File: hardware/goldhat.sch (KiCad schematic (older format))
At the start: 3 parts

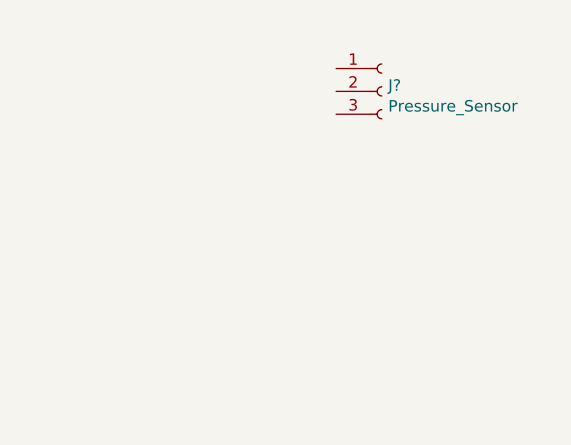
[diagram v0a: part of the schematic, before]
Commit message: added motor connectors
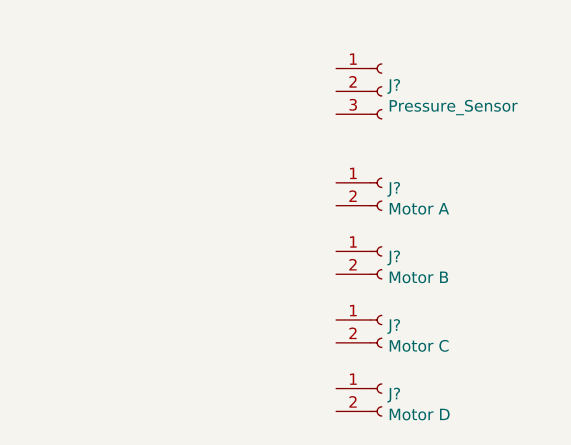
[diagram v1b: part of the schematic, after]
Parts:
- added J?: Motor A, symbol Connector:Conn_01x02_Female
- added J?: Motor B, symbol Connector:Conn_01x02_Female
- added J?: Motor C, symbol Connector:Conn_01x02_Female
- added J?: Motor D, symbol Connector:Conn_01x02_Female
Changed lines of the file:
@@
+	1    0    0    -1
+$EndComp
+$Comp
+L Connector:Conn_01x02_Female J?
+U 1 1 5E94AC7A
+P 9800 5200
+F 0 "J?" H 9828 5176 50  0000 L CNN
+F 1 "Motor A" H 9828 5085 50  0000 L CNN
+F 2 "" H 9800 5200 50  0001 C CNN
+F 3 "~" H 9800 5200 50  0001 C CNN
+	1    9800 5200
+	1    0    0    -1
+$EndComp
+$Comp
+L Connector:Conn_01x02_Female J?
+U 1 1 5E94B72C
+P 9800 5500
+F 0 "J?" H 9828 5476 50  0000 L CNN
+F 1 "Motor B" H 9828 5385 50  0000 L CNN
+F 2 "" H 9800 5500 50  0001 C CNN
+F 3 "~" H 9800 5500 50  0001 C CNN
+	1    9800 5500
+	1    0    0    -1
+$EndComp
+$Comp
+L Connector:Conn_01x02_Female J?
+U 1 1 5E94CD4B
+P 9800 5800
+F 0 "J?" H 9828 5776 50  0000 L CNN
+F 1 "Motor C" H 9828 5685 50  0000 L CNN
+F 2 "" H 9800 5800 50  0001 C CNN
+F 3 "~" H 9800 5800 50  0001 C CNN
+	1    9800 5800
+	1    0    0    -1
+$EndComp
+$Comp
+L Connector:Conn_01x02_Female J?
+U 1 1 5E94CD51
+P 9800 6100
+F 0 "J?" H 9828 6076 50  0000 L CNN
+F 1 "Motor D" H 9828 5985 50  0000 L CNN
+F 2 "" H 9800 6100 50  0001 C CNN
+F 3 "~" H 9800 6100 50  0001 C CNN
+	1    9800 6100
 	1    0    0    -1
 $EndComp

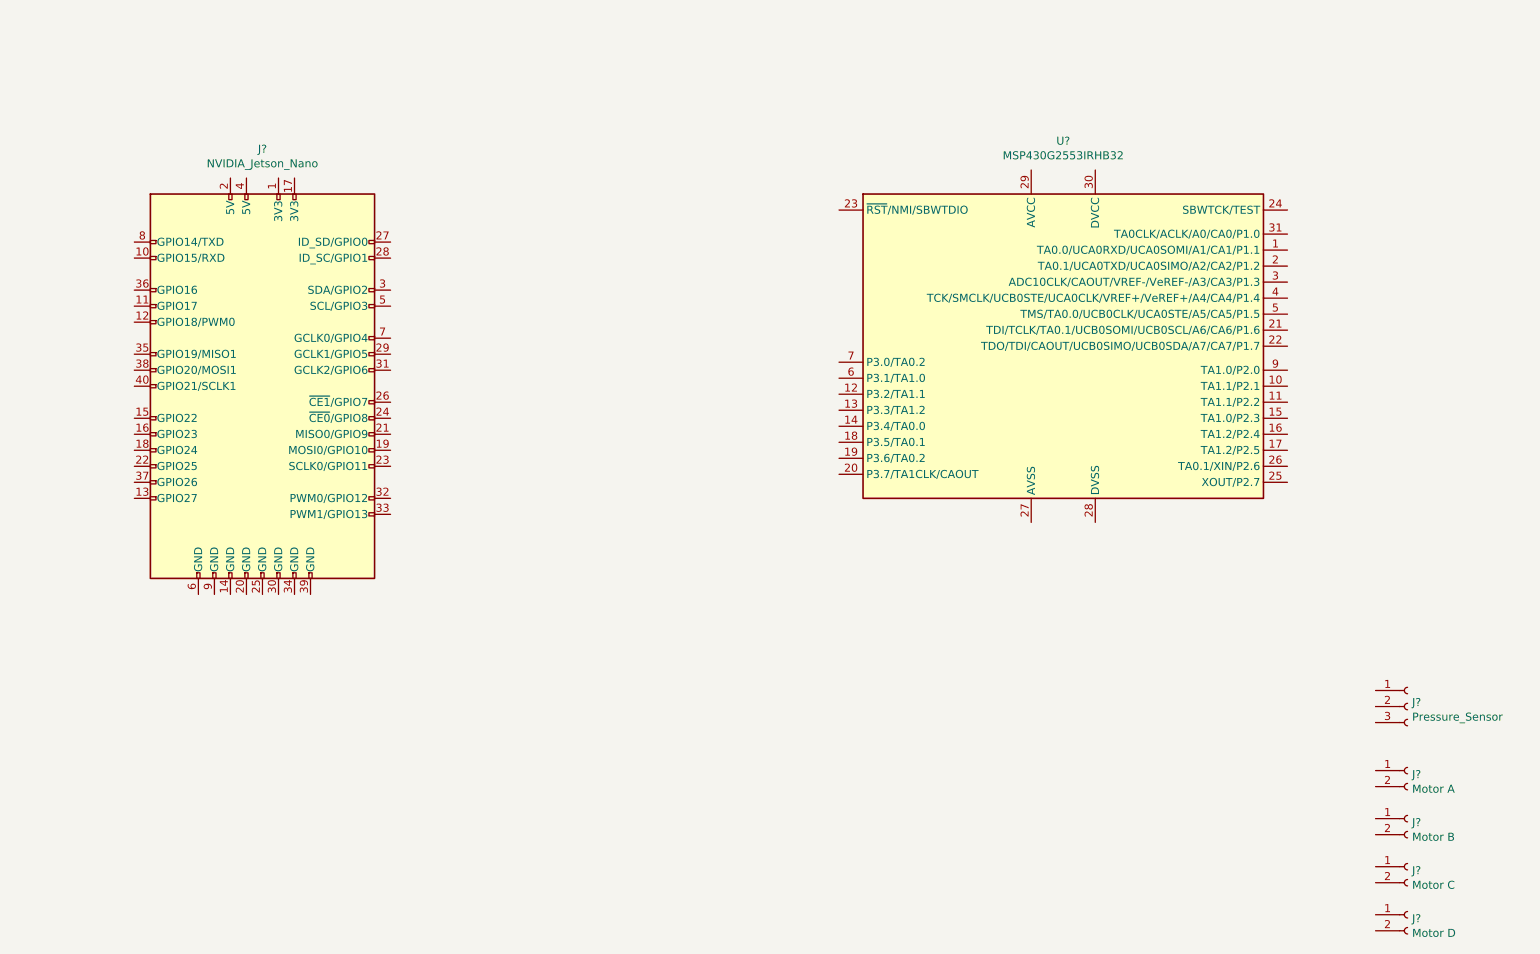
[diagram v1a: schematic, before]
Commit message: added hierarchical sheets because organizing
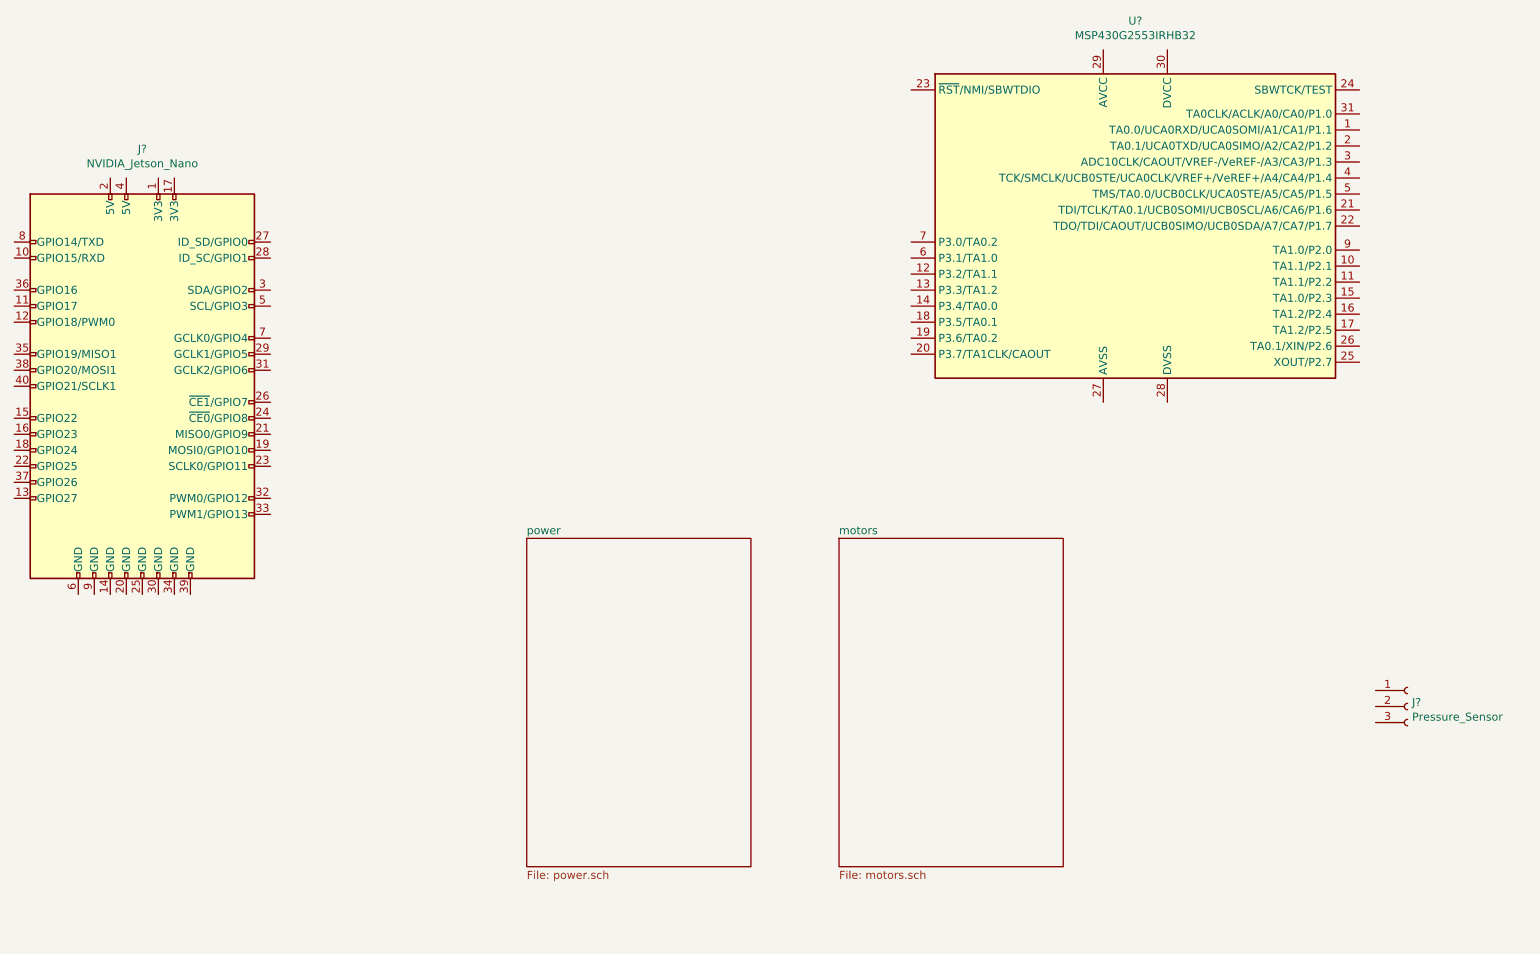
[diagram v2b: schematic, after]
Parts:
- removed J?: Motor A, symbol Connector:Conn_01x02_Female
- removed J?: Motor B, symbol Connector:Conn_01x02_Female
- removed J?: Motor C, symbol Connector:Conn_01x02_Female
- removed J?: Motor D, symbol Connector:Conn_01x02_Female
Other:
- moved on the sheet: J?, U?
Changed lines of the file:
@@
 $Descr A4 11693 8268
 encoding utf-8
-Sheet 1 1
+Sheet 1 3
 Title ""
 Date ""
@@
 L MCU_Texas_MSP430:MSP430G2553IRHB32 U?
 U 1 1 5E8F512E
-P 7650 2550
-F 0 "U?" H 7650 3831 50  0000 C CNN
-F 1 "MSP430G2553IRHB32" H 7650 3740 50  0000 C CNN
-F 2 "Package_DFN_QFN:Texas_S-PVQFN-N32_EP3.45x3.45mm" H 6500 1550 50  0001 C CIN
-F 3 "http://www.ti.com/lit/ds/symlink/msp430g2553.pdf" H 7650 2550 50  0001 C CNN
-	1    7650 2550
+P 8100 1800
+F 0 "U?" H 8100 3081 50  0000 C CNN
+F 1 "MSP430G2553IRHB32" H 8100 2990 50  0000 C CNN
+F 2 "Package_DFN_QFN:Texas_S-PVQFN-N32_EP3.45x3.45mm" H 6950 800 50  0001 C CIN
+F 3 "http://www.ti.com/lit/ds/symlink/msp430g2553.pdf" H 8100 1800 50  0001 C CNN
+	1    8100 1800
 	1    0    0    -1
 $EndComp
@@
 L Connector:Raspberry_Pi_2_3 J?
 U 1 1 5E8F67ED
-P 2650 2800
-F 0 "J?" H 2650 4281 50  0000 C CNN
-F 1 "NVIDIA_Jetson_Nano" H 2650 4190 50  0000 C CNN
-F 2 "" H 2650 2800 50  0001 C CNN
-F 3 "https://www.raspberrypi.org/documentation/hardware/raspberrypi/schematics/rpi_SCH_3bplus_1p0_reduced.pdf" H 2650 2800 50  0001 C CNN
-	1    2650 2800
+P 1900 2800
+F 0 "J?" H 1900 4281 50  0000 C CNN
+F 1 "NVIDIA_Jetson_Nano" H 1900 4190 50  0000 C CNN
+F 2 "" H 1900 2800 50  0001 C CNN
+F 3 "https://www.raspberrypi.org/documentation/hardware/raspberrypi/schematics/rpi_SCH_3bplus_1p0_reduced.pdf" H 1900 2800 50  0001 C CNN
+	1    1900 2800
 	1    0    0    -1
 $EndComp
@@
 	1    0    0    -1
 $EndComp
-$Comp
-L Connector:Conn_01x02_Female J?
-U 1 1 5E94AC7A
-P 9800 5200
-F 0 "J?" H 9828 5176 50  0000 L CNN
-F 1 "Motor A" H 9828 5085 50  0000 L CNN
-F 2 "" H 9800 5200 50  0001 C CNN
-F 3 "~" H 9800 5200 50  0001 C CNN
-	1    9800 5200
-	1    0    0    -1
-$EndComp
-$Comp
-L Connector:Conn_01x02_Female J?
-U 1 1 5E94B72C
-P 9800 5500
-F 0 "J?" H 9828 5476 50  0000 L CNN
-F 1 "Motor B" H 9828 5385 50  0000 L CNN
-F 2 "" H 9800 5500 50  0001 C CNN
-F 3 "~" H 9800 5500 50  0001 C CNN
-	1    9800 5500
-	1    0    0    -1
-$EndComp
-$Comp
-L Connector:Conn_01x02_Female J?
-U 1 1 5E94CD4B
-P 9800 5800
-F 0 "J?" H 9828 5776 50  0000 L CNN
-F 1 "Motor C" H 9828 5685 50  0000 L CNN
-F 2 "" H 9800 5800 50  0001 C CNN
-F 3 "~" H 9800 5800 50  0001 C CNN
-	1    9800 5800
-	1    0    0    -1
-$EndComp
-$Comp
-L Connector:Conn_01x02_Female J?
-U 1 1 5E94CD51
-P 9800 6100
-F 0 "J?" H 9828 6076 50  0000 L CNN
-F 1 "Motor D" H 9828 5985 50  0000 L CNN
-F 2 "" H 9800 6100 50  0001 C CNN
-F 3 "~" H 9800 6100 50  0001 C CNN
-	1    9800 6100
-	1    0    0    -1
-$EndComp
+$Sheet
+S 6250 3750 1400 2050
+U 5E94DDF9
+F0 "motors" 50
+F1 "motors.sch" 50
+$EndSheet
+$Sheet
+S 4300 3750 1400 2050
+U 5E94ECD4
+F0 "power" 50
+F1 "power.sch" 50
+$EndSheet
 $EndSCHEMATC

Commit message: changes on stream
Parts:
- added C?: C, symbol Device:C
- J1: renamed from J?; footprint (none) -> seniordesign:PinSocket_2x20_P2.54mm_Vertical_SMD_posts
- J2: renamed from J?; footprint (none) -> Connector_PinHeader_2.54mm:PinHeader_1x03_P2.54mm_Horizontal
- U1: renamed from U?; footprint Package_DFN_QFN:Texas_S-PVQFN-N32_EP3.45x3.45mm -> Package_DIP:DIP-32_W7.62mm
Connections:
- net +3V3: now reaches J1.1 (3V3)
- net +3V3: now also J1.17 (3V3)
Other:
- moved on the sheet: J1, U1
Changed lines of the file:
@@
 $EndDescr
 $Comp
-L MCU_Texas_MSP430:MSP430G2553IRHB32 U?
+L MCU_Texas_MSP430:MSP430G2553IRHB32 U1
 U 1 1 5E8F512E
-P 8100 1800
-F 0 "U?" H 8100 3081 50  0000 C CNN
-F 1 "MSP430G2553IRHB32" H 8100 2990 50  0000 C CNN
-F 2 "Package_DFN_QFN:Texas_S-PVQFN-N32_EP3.45x3.45mm" H 6950 800 50  0001 C CIN
-F 3 "http://www.ti.com/lit/ds/symlink/msp430g2553.pdf" H 8100 1800 50  0001 C CNN
-	1    8100 1800
+P 8100 2150
+F 0 "U1" H 8100 3431 50  0000 C CNN
+F 1 "MSP430G2553IRHB32" H 8100 3340 50  0000 C CNN
+F 2 "Package_DIP:DIP-32_W7.62mm" H 6950 1150 50  0001 C CIN
+F 3 "http://www.ti.com/lit/ds/symlink/msp430g2553.pdf" H 8100 2150 50  0001 C CNN
+	1    8100 2150
+	-1   0    0    -1
+$EndComp
+$Comp
+L Connector:Raspberry_Pi_2_3 J1
+U 1 1 5E8F67ED
+P 2050 3450
+F 0 "J1" H 2050 4931 50  0000 C CNN
+F 1 "NVIDIA_Jetson_Nano" H 2050 4840 50  0000 C CNN
+F 2 "seniordesign:PinSocket_2x20_P2.54mm_Vertical_SMD_posts" H 2050 3450 50  0001 C CNN
+F 3 "https://www.raspberrypi.org/documentation/hardware/raspberrypi/schematics/rpi_SCH_3bplus_1p0_reduced.pdf" H 2050 3450 50  0001 C CNN
+	1    2050 3450
 	1    0    0    -1
 $EndComp
 $Comp
-L Connector:Raspberry_Pi_2_3 J?
-U 1 1 5E8F67ED
-P 1900 2800
-F 0 "J?" H 1900 4281 50  0000 C CNN
-F 1 "NVIDIA_Jetson_Nano" H 1900 4190 50  0000 C CNN
-F 2 "" H 1900 2800 50  0001 C CNN
-F 3 "https://www.raspberrypi.org/documentation/hardware/raspberrypi/schematics/rpi_SCH_3bplus_1p0_reduced.pdf" H 1900 2800 50  0001 C CNN
-	1    1900 2800
-	1    0    0    -1
-$EndComp
-$Comp
-L Connector:Conn_01x03_Female J?
+L Connector:Conn_01x03_Female J2
 U 1 1 5E8F81AD
 P 9800 4800
-F 0 "J?" H 9828 4826 50  0000 L CNN
+F 0 "J2" H 9828 4826 50  0000 L CNN
 F 1 "Pressure_Sensor" H 9828 4735 50  0000 L CNN
-F 2 "" H 9800 4800 50  0001 C CNN
+F 2 "Connector_PinHeader_2.54mm:PinHeader_1x03_P2.54mm_Horizontal" H 9800 4800 50  0001 C CNN
 F 3 "~" H 9800 4800 50  0001 C CNN
 	1    9800 4800
@@
 F0 "motors" 50
 F1 "motors.sch" 50
+F2 "MotorAGo" I L 6250 4300 50
 $EndSheet
 $Sheet
@@
 F1 "power.sch" 50
 $EndSheet
+$Comp
+L Device:C C?
+U 1 1 5E9AAE09
+P 3500 1300
+F 0 "C?" H 3615 1346 50  0000 L CNN
+F 1 "C" H 3615 1255 50  0000 L CNN
+F 2 "" H 3538 1150 50  0001 C CNN
+F 3 "~" H 3500 1300 50  0001 C CNN
+	1    3500 1300
+	1    0    0    -1
+$EndComp
+$Comp
+L power:+3.3V #PWR?
+U 1 1 5E9AC293
+P 2250 1950
+F 0 "#PWR?" H 2250 1800 50  0001 C CNN
+F 1 "+3.3V" H 2265 2123 50  0000 C CNN
+F 2 "" H 2250 1950 50  0001 C CNN
+F 3 "" H 2250 1950 50  0001 C CNN
+	1    2250 1950
+	1    0    0    -1
+$EndComp
+Wire Wire Line
+	2250 1950 2250 2050
+Wire Wire Line
+	2250 2050 2150 2050
+Wire Wire Line
+	2150 2050 2150 2150
+Connection ~ 2250 2050
+Wire Wire Line
+	2250 2050 2250 2150
 $EndSCHEMATC
